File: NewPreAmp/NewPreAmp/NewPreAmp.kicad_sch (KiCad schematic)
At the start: 1 part, among them U1 TPS65131TRGERQ1

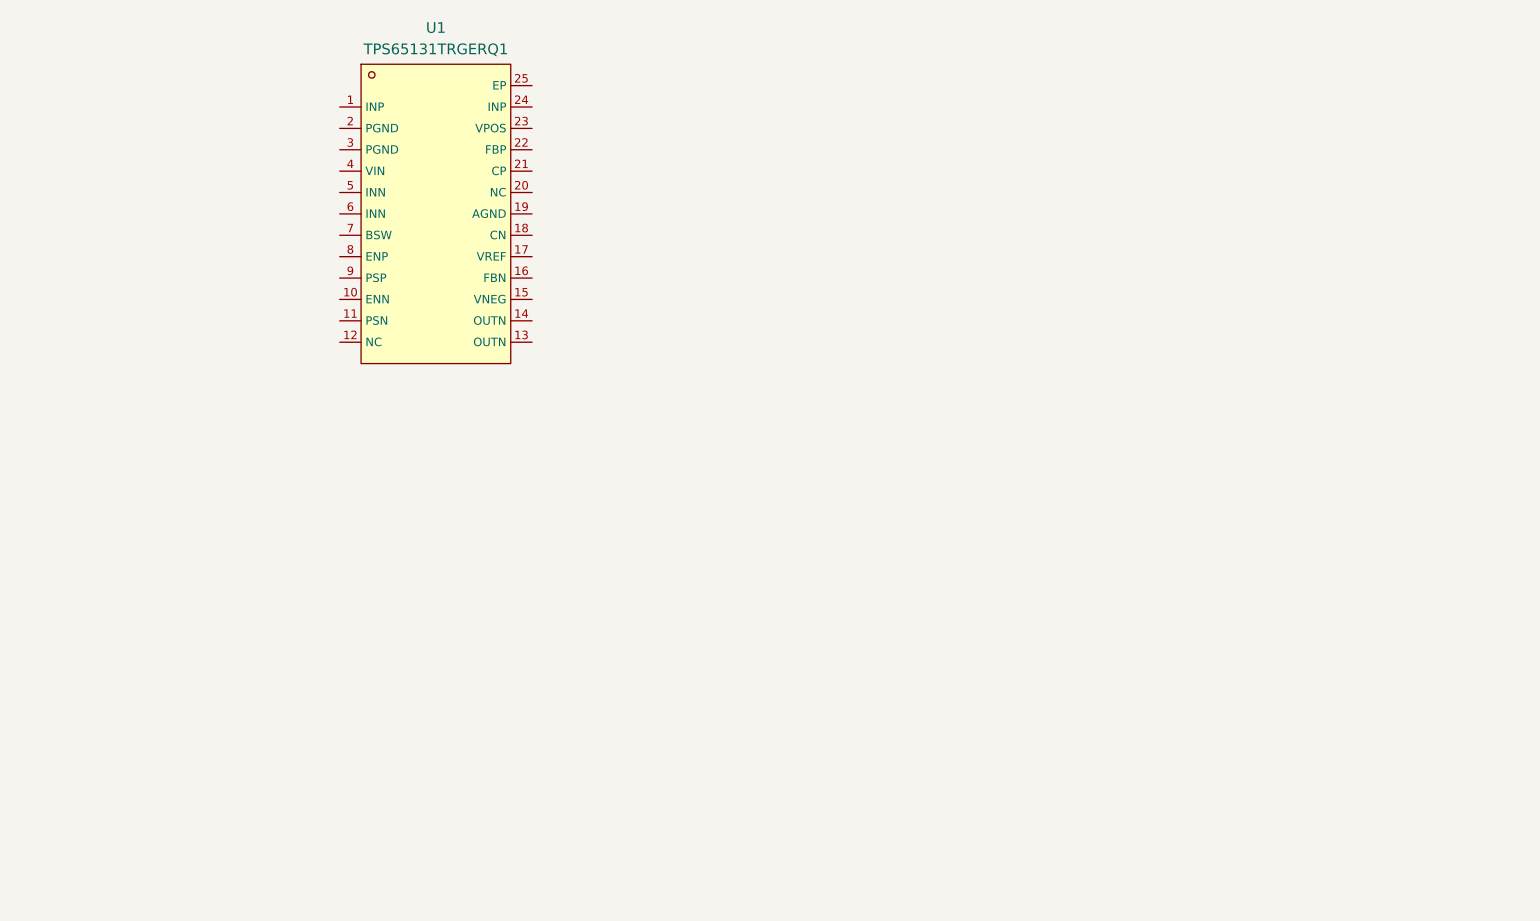
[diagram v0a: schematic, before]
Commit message: Added USB-C and +-12v IC
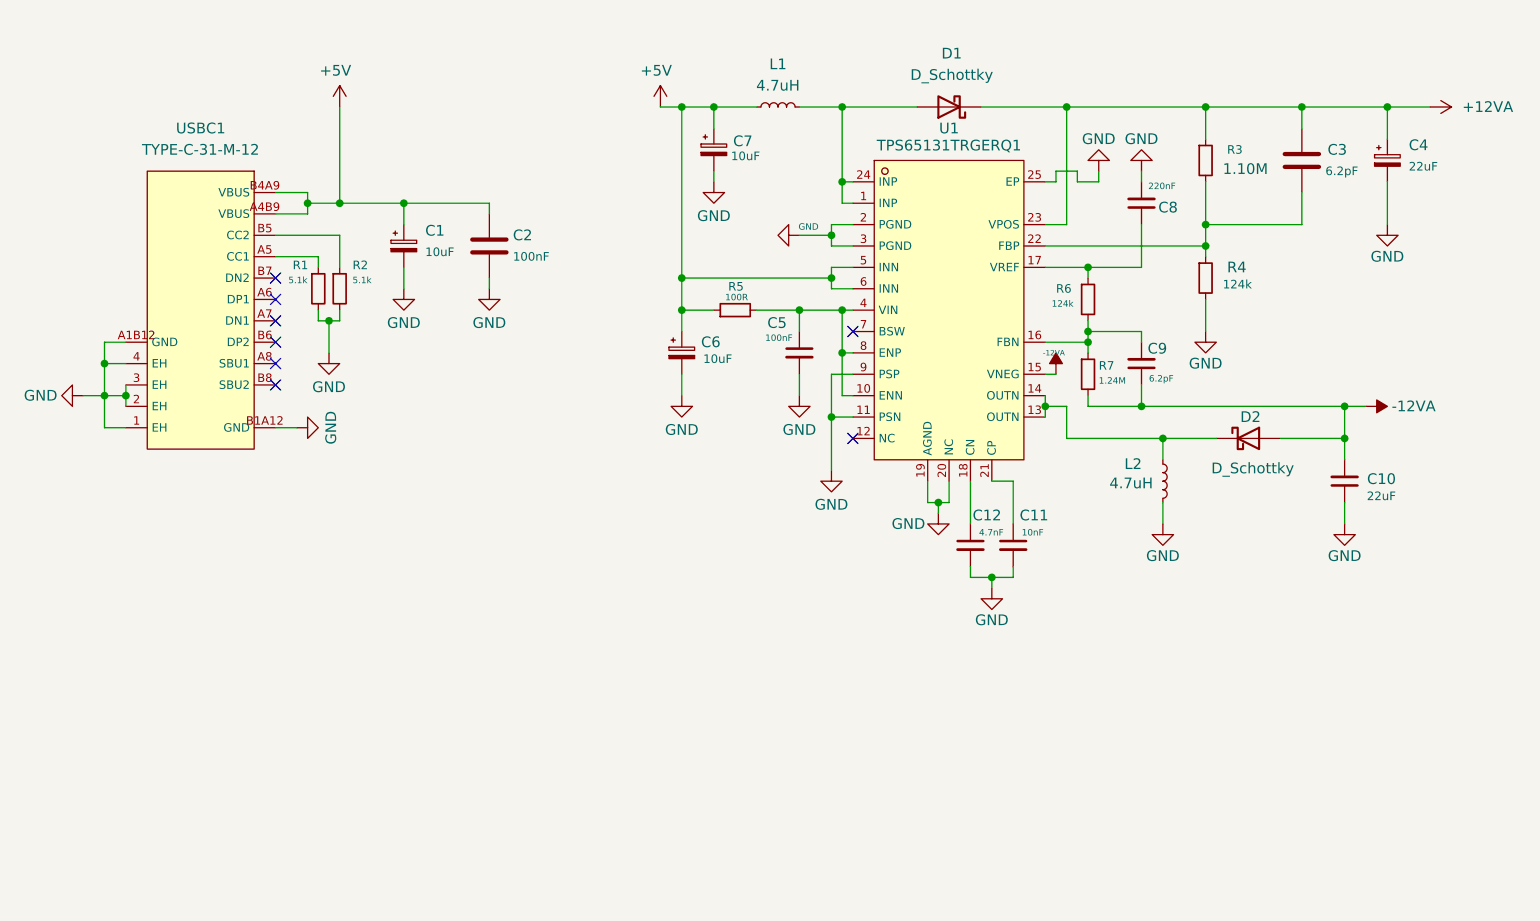
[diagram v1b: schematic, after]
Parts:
- added C1, C6, C7: 10uF, symbol Device:C_Polarized_Small
- added C10: 22uF, symbol Device:C_Small
- added C11: 10nF, symbol Device:C_Small
- added C12: 4.7nF, symbol Device:C_Small
- added C2: 100nF, symbol Device:C
- added C3: 6.2pF, symbol Device:C
- added C4: 22uF, symbol Device:C_Polarized_Small
- added C5: 100nF, symbol Device:C_Small
- added C8: 220nF, symbol Device:C_Small
- added C9: 6.2pF, symbol Device:C_Small
- added D1, D2: D_Schottky, symbol Device:D_Schottky
- added L1, L2: 4.7uH, symbol Device:L_Small
- added R1, R2: 5.1k, symbol Device:R_Small
- added R3: 1.10M, symbol Device:R_Small
- added R4, R6: 124k, symbol Device:R_Small
- added R5: 100R, symbol Device:R_Small
- added R7: 1.24M, symbol Device:R_Small
- added USBC1: TYPE-C-31-M-12, lcsc_footprints:C165948_USB-C_SMD-TYPE-C-31-M-12_1, symbol lcsc_imported:TYPE-C-31-M-12
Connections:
- net at U1.1 (INP): now also U1.24 (INP), D1.2 (A), L1.2
- net at U1.10 (ENN): now also U1.4 (VIN), U1.8 (ENP), C5.1, R5.2
- net GND: now reaches U1.11 (PSN)
- net GND: now also U1.19 (AGND), U1.2 (PGND), U1.20 (NC), U1.25 (EP), U1.3 (PGND), U1.9 (PSP), C1.2, C10.1, C11.2, C12.2, C2.2, C4.2, C5.2, C6.2, C7.2, C8.2, L2.2, R1.2, R2.2, R4.2, USBC1.1 (EH), USBC1.2 (EH), USBC1.3 (EH), USBC1.4 (EH), USBC1.A1B12 (GND), USBC1.B1A12 (GND)
- net at U1.13 (OUTN): now also U1.14 (OUTN), D2.1 (K), L2.1
- net -12VA: now reaches U1.15 (VNEG)
- net -12VA: now also C10.2, C9.1, D2.2 (A), R7.2
- net at U1.16 (FBN): now also C9.2, R6.2, R7.1
- net at U1.17 (VREF): now also C8.1, R6.1
- net at U1.18 (CN): now also C12.1
- net at U1.21 (CP): now also C11.1
- net at U1.22 (FBP): now also C3.2, R3.2, R4.1
- net +12VA: now reaches U1.23 (VPOS)
- net +12VA: now also C3.1, C4.1, D1.1 (K), R3.1
- net +5V: now reaches U1.5 (INN)
- net +5V: now also U1.6 (INN), C1.1, C2.1, C6.1, C7.1, L1.1, R5.1, USBC1.A4B9 (VBUS), USBC1.B4A9 (VBUS)
- new net: R1.1, USBC1.A5 (CC1)
- new net: R2.1, USBC1.B5 (CC2)
- no-connect marks 0 -> 8
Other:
- moved on the sheet: U1

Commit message: Updated repo's name
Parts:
- added U2: OPA1612AIDR, lcsc_footprints:C94590_SOIC-8_L5_0-W4_0-P1_27-LS6_0-BL, symbol lcsc_imported:OPA1612AIDR
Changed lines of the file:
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@@
+	)
+	(symbol
+		(lib_id "lcsc_imported:OPA1612AIDR")
+		(at 62.738 126.492 0)
+		(unit 1)
+		(exclude_from_sim no)
+		(in_bom yes)
+		(on_board yes)
+		(dnp no)
+		(fields_autoplaced yes)
+		(property "Reference" "U2"
+			(at 61.468 116.84 0)
+			(effects
+				(font
+					(size 1.27 1.27)
+				)
+			)
+		)
+		(property "Value" "OPA1612AIDR"
+			(at 61.468 119.38 0)
+			(effects
+				(font
+					(size 1.27 1.27)
+				)
+			)
+		)
+		(property "Footprint" "lcsc_footprints:C94590_SOIC-8_L5_0-W4_0-P1_27-LS6_0-BL"
+			(at 62.738 136.652 0)
+			(effects
+				(font
+					(size 1.27 1.27)
+				)
+				(hide yes)
+			)
+		)
+		(property "Datasheet" "https://www.lcsc.com/datasheet/lcsc_datasheet_2304140030_Texas-Instruments-OPA1612AIDR_C94590.pdf"
+			(at 60.452 126.365 0)
+			(effects
+				(font
+					(size 1.27 1.27)
+				)
+				(hide yes)
+			)
+		)
+		(property "Description" "OPA1612AIDR"
+			(at 62.738 126.492 0)
+			(effects
+				(font
+					(size 1.27 1.27)
+				)
+				(hide yes)
+			)
+		)
+		(property "LCSC" "C94590"
+			(at 62.738 126.492 0)
+			(effects
+				(font
+					(size 1.27 1.27)
+				)
+				(hide yes)
+			)
+		)
+		(property "Manufacturer" "TI(德州仪器)"
+			(at 62.738 126.492 0)
+			(effects
+				(font
+					(size 1.27 1.27)
+				)
+				(hide yes)
+			)
+		)
+		(pin "6"
+		)
+		(pin "7"
+		)
+		(pin "8"
+		)
+		(pin "4"
+		)
+		(pin "5"
+		)
+		(pin "1"
+		)
+		(pin "3"
+		)
+		(pin "2"
+		)
+		(instances
+			(project ""
+				(path "/586e244e-6659-4934-b4de-ab0cd4bc380d"
+					(reference "U2")
+					(unit 1)
+				)
+			)
+		)
 	)
 	(symbol
